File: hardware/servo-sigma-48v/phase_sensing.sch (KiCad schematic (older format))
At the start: 31 parts, among them U10 OPA4374, U9 OPA4374

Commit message: Finished routing of the servo controller
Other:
- moved on the sheet: U10A, U10B, U10C, U10D

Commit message: Updated the footprints
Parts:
- C11, C44, C45, C46: footprint Capacitors_SMD:C_0805 -> Capacitor_SMD:C_0805_2012Metric; symbol device:C -> servo-sigma-48v-rescue:C-device
- C43: footprint Capacitors_SMD:C_0603 -> Capacitor_SMD:C_0603_1608Metric; symbol device:C -> servo-sigma-48v-rescue:C-device
- R16, R21, R31, R41, R45, R46, R48, R49, R51, R52, R57, R58, R59, R60, R61, R62, R63, R64, R65, R66, R70, R71, R72, R73: footprint Resistors_SMD:R_0603 -> Resistor_SMD:R_0603_1608Metric; symbol device:R -> servo-sigma-48v-rescue:R-device
- U10, U9: footprint Housings_SOIC:SOIC-14_3.9x8.7mm_Pitch1.27mm -> Package_SO:SOIC-14_3.9x8.7mm_P1.27mm

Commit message: work on rs485
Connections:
- net A_ISENSE_N: now also R71.1; no longer R41.1
- net A_ISENSE_P: now also R70.1; no longer R31.1
- net C_ISENSE_N: now also R41.1; no longer R64.1
- net C_ISENSE_P: now also R31.1; no longer R63.1
- net IA_FB: now also R73.2, U9.14; no longer R58.2, U9.1
- net IC_FB: now also R58.2, U9.1; no longer R66.2, U9.8
- net IR_FB: now also R66.2, U9.8; no longer R73.2, U9.14
- net R_ISENSE_N: now also R64.1; no longer R71.1
- net R_ISENSE_P: now also R63.1; no longer R70.1
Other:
- moved on the sheet: C11, C44, R57, R61, R63, R64, R66, R70, R71, R73, U10A, U10B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

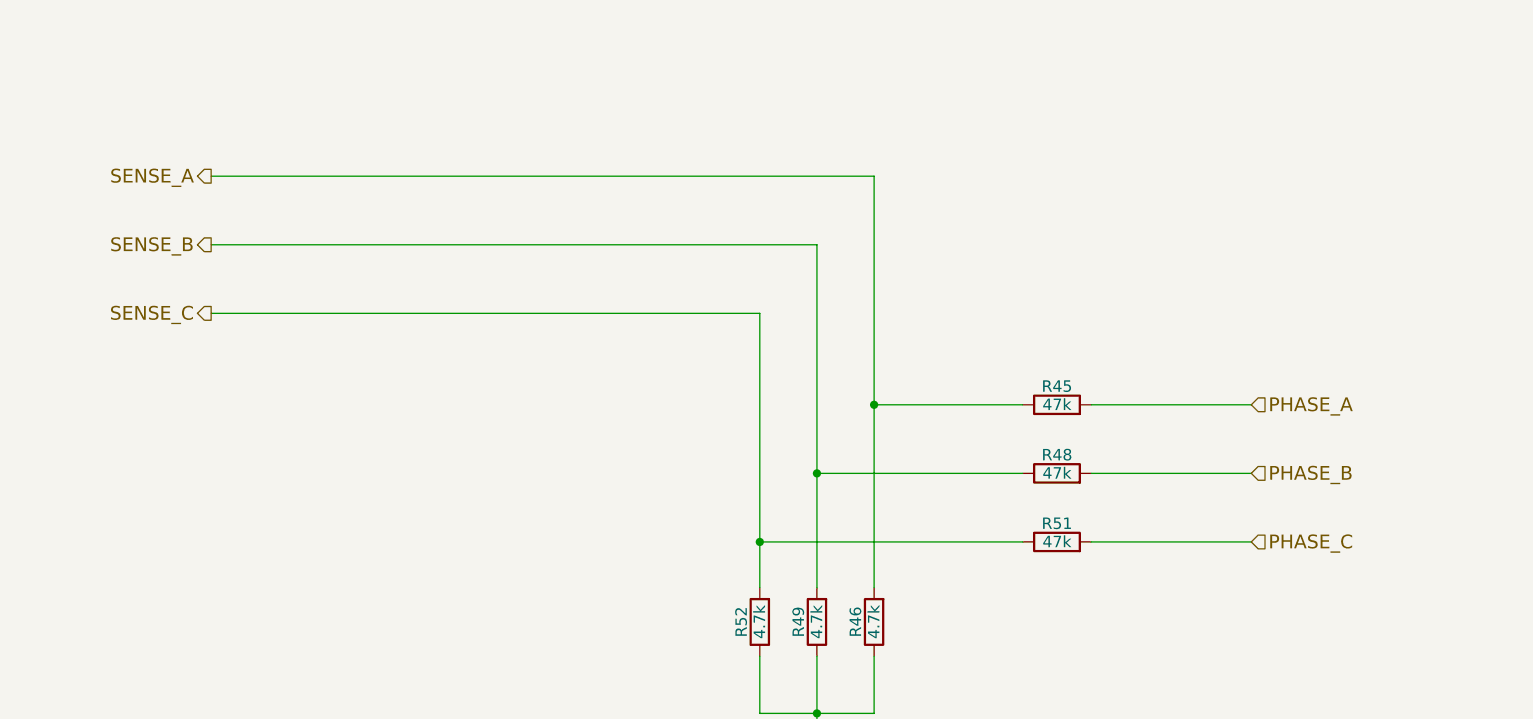
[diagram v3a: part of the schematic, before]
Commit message: Changed the MCU to use 100 pin
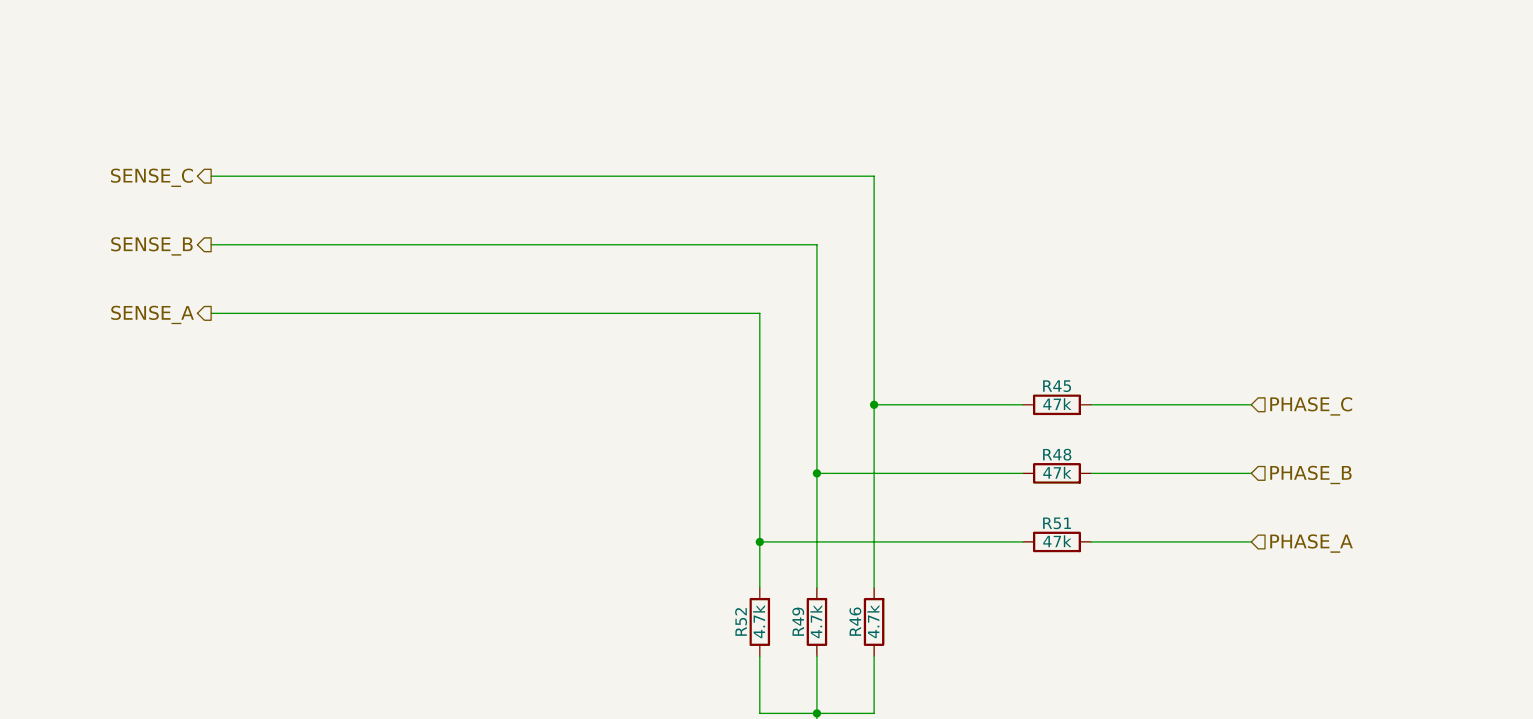
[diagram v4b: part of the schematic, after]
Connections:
- net PHASE_A: now also R51.2; no longer R45.2
- net PHASE_C: now also R45.2; no longer R51.2
- net SENSE_A: now also R51.1, R52.2; no longer R45.1, R46.2
- net SENSE_C: now also R45.1, R46.2; no longer R51.1, R52.2
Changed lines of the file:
@@
 Comment4 ""
 $EndDescr
-Text HLabel 6250 9400 2    60   Input ~ 0
+Text HLabel 6250 10000 2    60   Input ~ 0
 PHASE_A
 Text HLabel 6250 9700 2    60   Input ~ 0
 PHASE_B
-Text HLabel 6250 10000 2    60   Input ~ 0
+Text HLabel 6250 9400 2    60   Input ~ 0
 PHASE_C
 $Comp
@@
 	1    0    0    -1
 $EndComp
-Text HLabel 1700 9000 0    60   Output ~ 0
+Text HLabel 1700 8400 0    60   Output ~ 0
 SENSE_C
 Text HLabel 1700 8700 0    60   Output ~ 0
 SENSE_B
-Text HLabel 1700 8400 0    60   Output ~ 0
+Text HLabel 1700 9000 0    60   Output ~ 0
 SENSE_A
 $Comp

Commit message: Work on verson 2.0
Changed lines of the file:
@@
 C_ISENSE_N
 Wire Wire Line
-	13000 2250 13250 2250
-Wire Wire Line
-	13000 2450 13250 2450
+	12900 2250 13250 2250
+Wire Wire Line
+	12900 2450 13250 2450
 Text HLabel 4850 2350 2    60   Output ~ 0
 IC_FB
@@
 	-1   0    0    1
 $EndComp
-Text HLabel 13000 2250 0    60   Input ~ 0
+Text HLabel 12900 2250 0    60   Input ~ 0
 R_ISENSE_P
-Text HLabel 13000 2450 0    60   Input ~ 0
+Text HLabel 12900 2450 0    60   Input ~ 0
 R_ISENSE_N
 Wire Wire Line
@@
 Wire Wire Line
 	8750 6550 12300 6550
+Text Label 12950 2250 0    60   ~ 0
+RS_P
+Text Label 12950 2450 0    60   ~ 0
+RS_N
 $EndSCHEMATC

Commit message: completed routing
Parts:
- removed C11, C44, C45, C46: 4.7uF 25V, Capacitor_SMD:C_0805_2012Metric, symbol servo-sigma-48v-rescue:C-device
- removed C43: 100nF 50V, Capacitor_SMD:C_0603_1608Metric, symbol servo-sigma-48v-rescue:C-device
- removed R16, R21: 10k, Resistor_SMD:R_0603_1608Metric, symbol servo-sigma-48v-rescue:R-device
- removed R31, R41, R59, R60, R63, R64, R70, R71: 1.0k 0.1%, Resistor_SMD:R_0603_1608Metric, symbol servo-sigma-48v-rescue:R-device
- removed R57, R58, R61, R62, R65, R66, R72, R73: 10k 0.1%, Resistor_SMD:R_0603_1608Metric, symbol servo-sigma-48v-rescue:R-device
- removed U10, U9: OPA4374, Package_SO:SOIC-14_3.9x8.7mm_P1.27mm, symbol sigmadrone:OPA4374
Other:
- note removed: "Originally 2.2uF"
- moved on the sheet: R45, R46, R48, R49, R51, R52
